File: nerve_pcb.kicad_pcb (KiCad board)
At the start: 6 copper layers, 50 x 50 mm, 81 parts, among them J1 TC2050-IDC, J2 2171750001, J4 472192001, J5 BF030-16A-B1-0360-0277-0600-LB, J6 BF080-20-A-1-L-C, J7 UART, J8 CAN1, J9 CAN2, SW1 SPST, SW2 SPST, U1 ld39150dt33-r, U2 STM32F446RET, U3 TXB0104QPWRQ1, U4 BNO085, U5 BMP390, U6 TJA1051T/3, U7 TJA1051T/3, Y1 8M, Y2 32k768, Y3 32k768

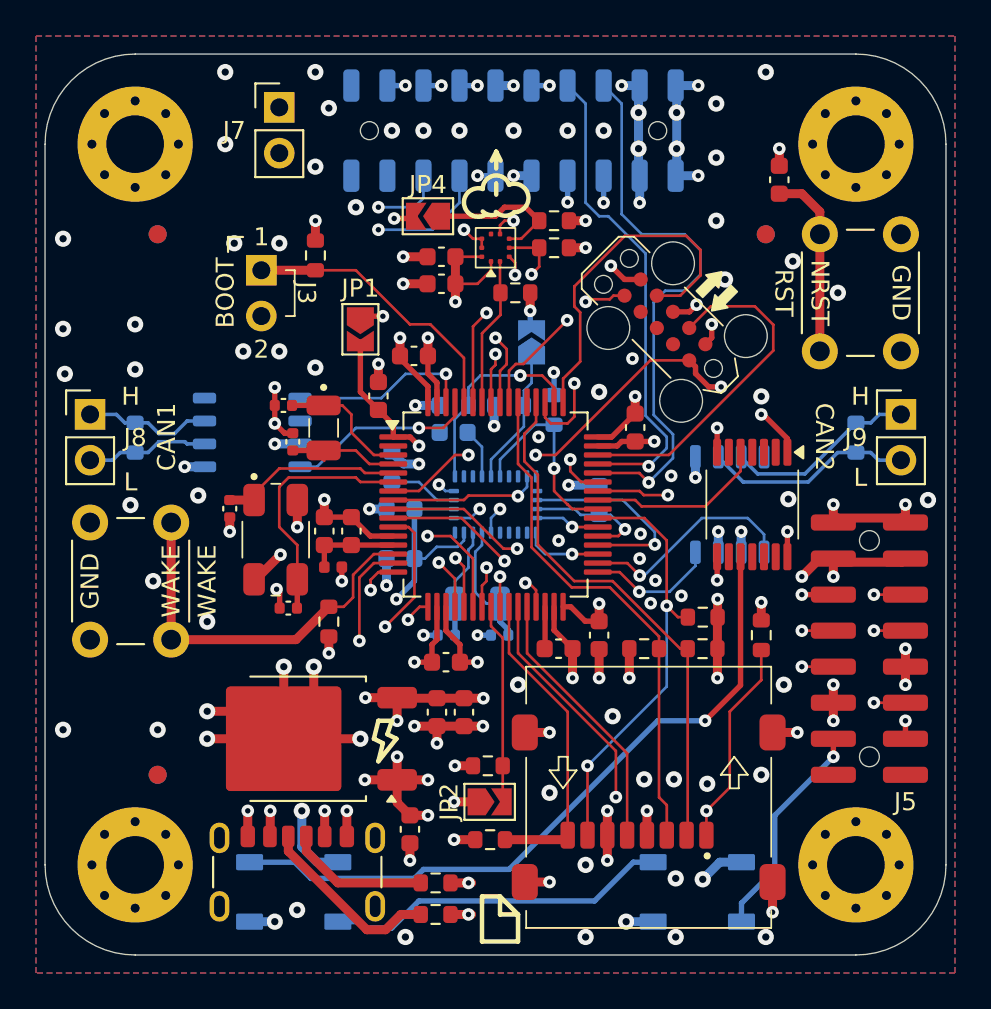
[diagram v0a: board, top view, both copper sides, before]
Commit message: Fix BNO085 circuit and touchups
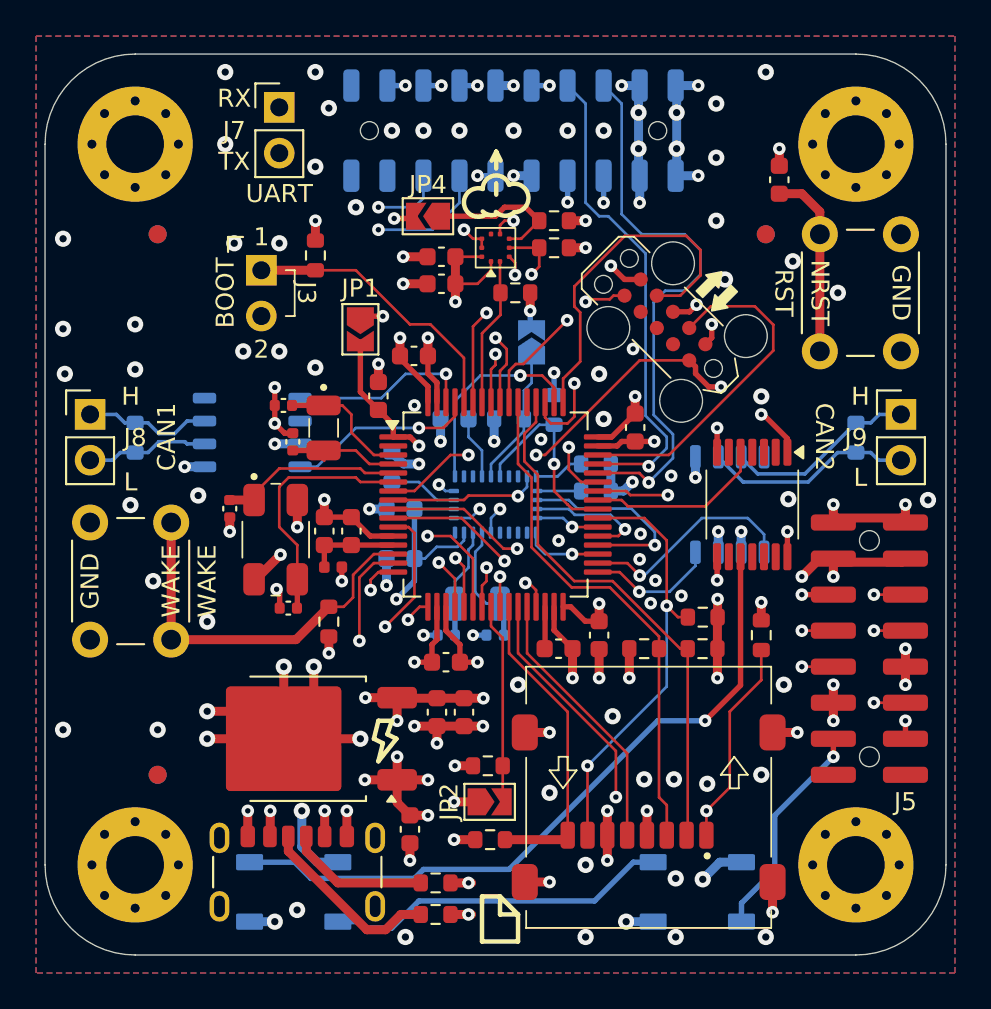
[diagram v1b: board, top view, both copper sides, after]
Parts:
- removed the R11 at (154.2, 104.8)
- added R14: 2k2, Resistor_SMD:R_0603_1608Metric, B.Cu at (154.1, 102.8)
- R15: value 10k -> 2k2
- moved R15 9.22 mm to (154.1, 104.2)
- moved C21 0.75 mm to (146.2, 100.2)
- moved R13 0.75 mm to (149.2, 100.2)
- moved C19 0.25 mm to (148.5, 112.2)
- turned Y3 to 180 degrees
- renumbered C20 to C19, C19 to C20, R13 to R11, R14 to R13
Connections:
- R15 pad 1: /GPIO_IMU_P0 -> +3V3
- R15 pad 2: GND -> Net-(U4-ENV_SDA)
- U4 pad 15: unconnected-(U4-ENV_SCL-Pad15) -> Net-(U4-ENV_SCL)
- U4 pad 16: unconnected-(U4-ENV_SDA-Pad16) -> Net-(U4-ENV_SDA)
- Y3 pad 1: Net-(U4-XIN32) -> Net-(U4-XOUT32/CLKSEL1)
- Y3 pad 2: Net-(U4-XOUT32/CLKSEL1) -> Net-(U4-XIN32)
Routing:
- net Net-(U4-ENV_SCL): track 0.00 -> 2.78 mm
- net Net-(U4-ENV_SDA): track 0.00 -> 2.44 mm
- net +3V3: track 88.7 -> 89.9 mm
- net Net-(U4-CAP): track 2.77 -> 3.50 mm
- net GND: track 102.8 -> 102.9 mm, vias 123 -> 125
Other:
- board text added: "RX"
- board text added: "TX"
- board text added: "UART"

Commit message: Major cleanup and add missing transfer vias
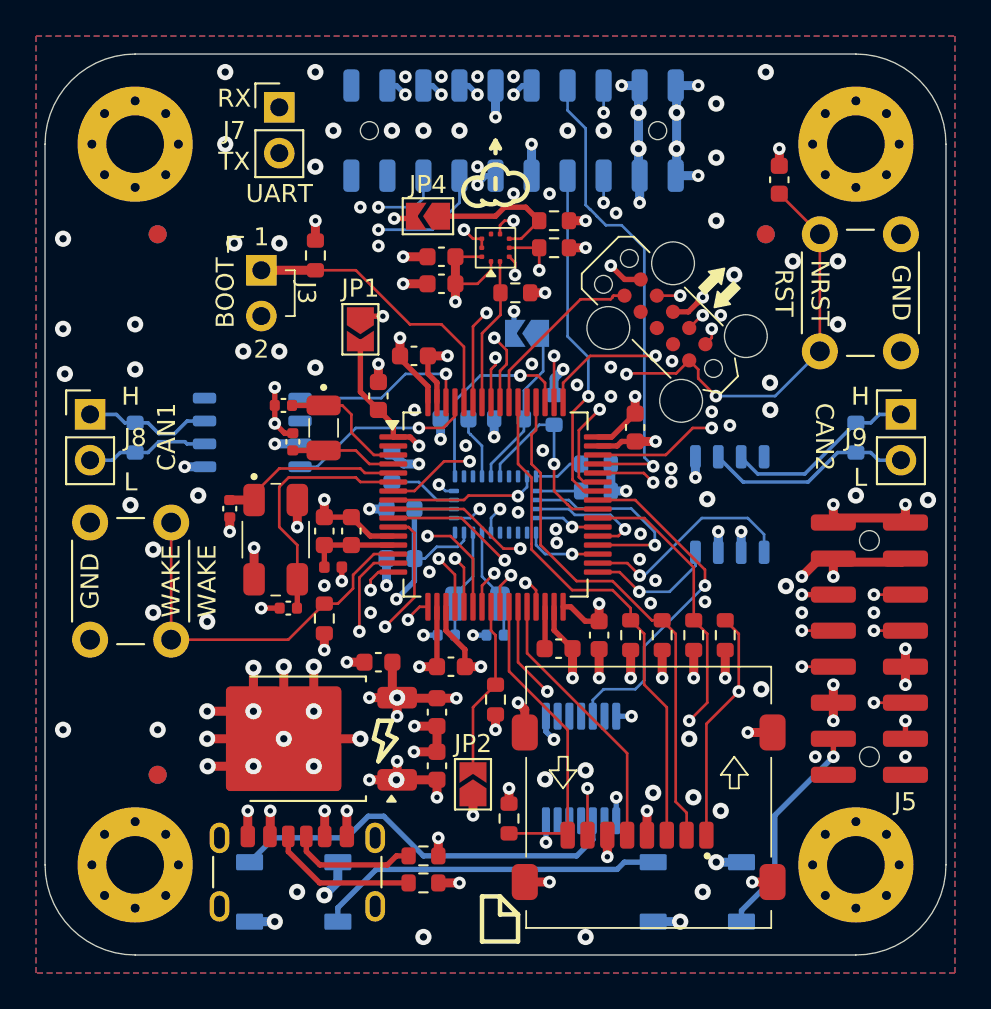
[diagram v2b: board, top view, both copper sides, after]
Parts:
- U3: moved to B.Cu
- moved U3 17.5 mm to (153.2, 119.7)
- moved C9 5.50 mm to (142.0, 113.8), turned to 180 degrees
- moved C3 3.83 mm to (145.2, 119.5), turned to 90 degrees
- moved R10 3.70 mm to (148.5, 115.8), turned to -90 degrees
- moved R7 2.36 mm to (157.8, 112.2), turned to 90 degrees
- moved R8 2.00 mm to (161.2, 112.2), turned to 90 degrees
- moved R2 1.88 mm to (144.5, 126.0)
- moved R1 1.64 mm to (144.5, 124.5)
- moved R4 1.58 mm to (149.2, 122.4), turned to -90 degrees
- moved JP2 1.34 mm to (147.2, 120.5), turned to 90 degrees
- moved R5 1.12 mm to (159.5, 112.2), turned to 90 degrees
- moved R6 1.06 mm to (156.0, 112.2), turned to 90 degrees
- moved JP3 0.56 mm to (150.2, 95.5), turned to 180 degrees
- moved C5 0.37 mm to (146.0, 114.0)
- moved R3 0.31 mm to (139.0, 111.3)
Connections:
- J6 pad 6: /USART1_TX -> /USART1_RX
- J6 pad 8: /USART1_RX -> /USART1_TX
- U2 pad 50: /GPIO_IMU_P0 -> /GPIO_RADIO_RST
- U2 pad 51: /GPIO_RADIO_RST -> /GPIO_IMU_P0
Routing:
- net /TIM1_CH1_PWM_{5V}: track 39.2 -> 22.4 mm, vias 1 -> 0
- net /TIM1_CH1_PWM: track 9.93 -> 19.3 mm, vias 0 -> 1
- net /SWCLK: track 19.7 -> 12.0 mm, vias 0 -> 2
- net +5V: track 35.4 -> 29.6 mm
- net /USART1_CTS: track 31.4 -> 26.7 mm, vias 1 -> 2
- net /USART1_TX: track 24.0 -> 19.4 mm, vias 2 -> 1
- net /SWDIO: track 19.2 -> 15.3 mm, vias 0 -> 2
- net /GPIO_RADIO_RST: track 22.7 -> 19.2 mm
- net GND: track 102.9 -> 106.2 mm, vias 125 -> 155
- net +3V3: track 89.9 -> 87.1 mm, vias 38 -> 40
- net Net-(J2-CC1): track 10.3 -> 8.24 mm
- net /USART2_TX: track 36.1 -> 34.2 mm
- net Net-(JP3-A): track 7.64 -> 9.31 mm
- net /SDIO_D0: track 24.0 -> 25.5 mm
- net /SDIO_DET: track 11.1 -> 9.75 mm
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
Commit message: Cleanup silkscreen
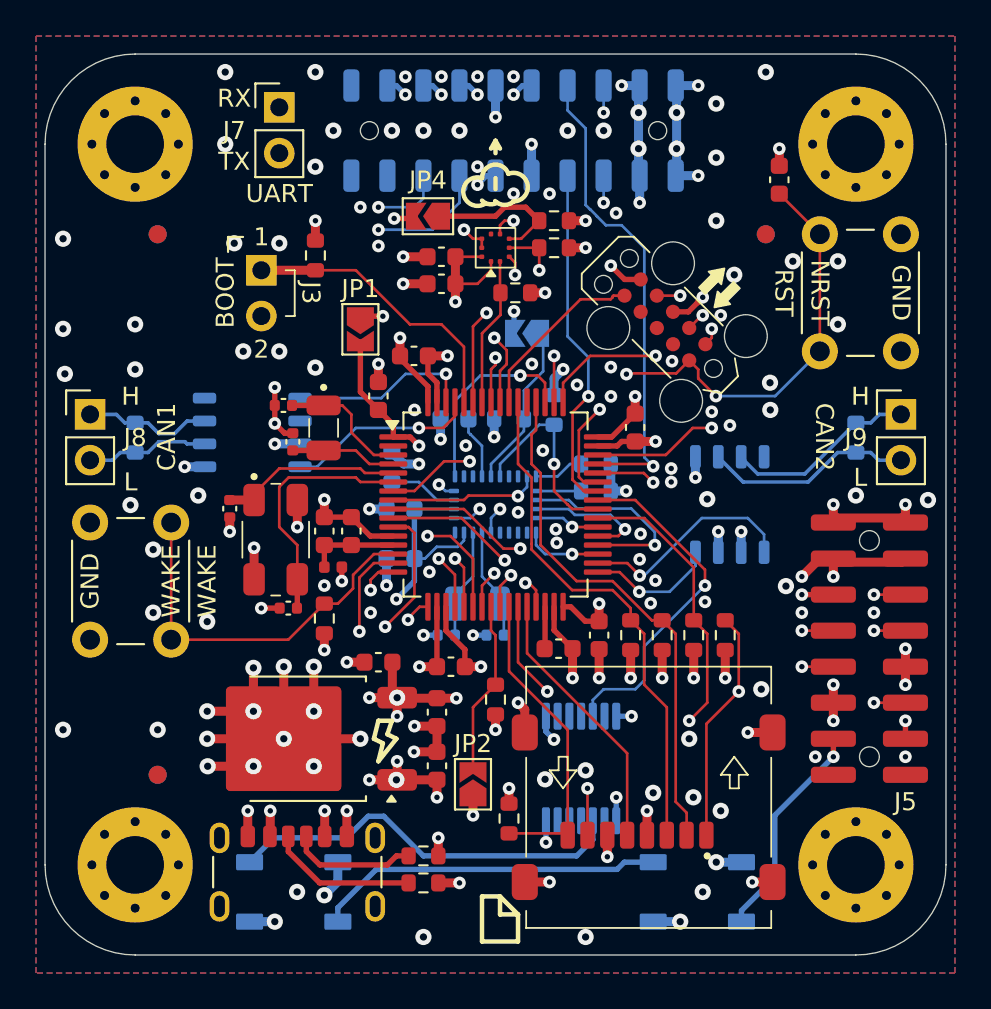
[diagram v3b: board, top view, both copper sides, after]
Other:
- board text added: "Daniel Jeon nerve_pcb v0.1.0-beta"
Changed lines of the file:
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@@
 		(tags "solder jumper open")
 		(property "Reference" "JP1"
-			(at -2.275 0 0)
+			(at -2.25 0 0)
 			(layer "F.SilkS")
 			(effects
@@
 		(tags "solder jumper open")
 		(property "Reference" "JP4"
-			(at 0 1.75 180)
+			(at 0 2 180)
 			(layer "F.SilkS")
 			(effects
@@
 		(tags "resistor")
 		(property "Reference" "R1"
-			(at 2.5 0 360)
+			(at 2.5 0 0)
 			(layer "F.SilkS")
 			(hide yes)
@@
 		)
 		(property "Value" "5k1"
-			(at 2.575 0 360)
+			(at 2.575 0 0)
 			(layer "F.Fab")
 			(effects
@@
 		)
 		(fp_text user "${REFERENCE}"
-			(at 0 0 360)
+			(at 0 0 0)
 			(layer "F.Fab")
 			(effects
@@
 				(font
 					(size 1 1)
-					(thickness 0.1)
+					(thickness 0.15)
 				)
 			)
@@
 		(tags "capacitor")
 		(property "Reference" "C9"
-			(at 2.5 0 360)
+			(at 2.5 0 0)
 			(layer "F.SilkS")
 			(hide yes)
@@
 		)
 		(property "Value" "4u7"
-			(at 2.5 0 360)
+			(at 2.5 0 0)
 			(layer "F.Fab")
 			(effects
@@
 		)
 		(fp_text user "${REFERENCE}"
-			(at 0 0 360)
+			(at 0 0 0)
 			(layer "F.Fab")
 			(effects
@@
 		(at 135.505 93.27 -90)
 		(property "Reference" "J3"
-			(at -0.02 -2.5 -90)
+			(at -0.02 -2.745 -90)
 			(unlocked yes)
 			(layer "F.SilkS")
@@
 				(font
 					(size 1 1)
-					(thickness 0.1)
+					(thickness 0.15)
 				)
 			)
@@
 		(tags "solder jumper open")
 		(property "Reference" "JP3"
-			(at 2.25 0 90)
+			(at 0.25 2 180)
 			(layer "B.SilkS")
 			(effects
@@
 		)
 		(property "Value" "Open"
-			(at 0 0 360)
+			(at 0 0 0)
 			(layer "B.Fab")
 			(effects
@@
 				(font
 					(size 1 1)
-					(thickness 0.1)
+					(thickness 0.15)
 				)
 				(justify mirror)
@@
 	)
 	(gr_text "GND"
-		(at 126 109.25 -90)
+		(at 126 109.25 90)
 		(layer "B.SilkS")
 		(effects
@@
 	)
 	(gr_text "WAKE"
-		(at 130.5 109.25 -90)
+		(at 130.5 109.25 90)
 		(layer "B.SilkS")
 		(effects
@@
 		)
 	)
+	(gr_text "Daniel Jeon\nnerve_pcb\nv0.1.0-beta"
+		(at 148.5 128.75 0)
+		(layer "B.SilkS")
+		(effects
+			(font
+				(size 1 1)
+				(thickness 0.2)
+				(bold yes)
+			)
+			(justify bottom mirror)
+		)
+	)

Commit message: Switch to split CAN termination
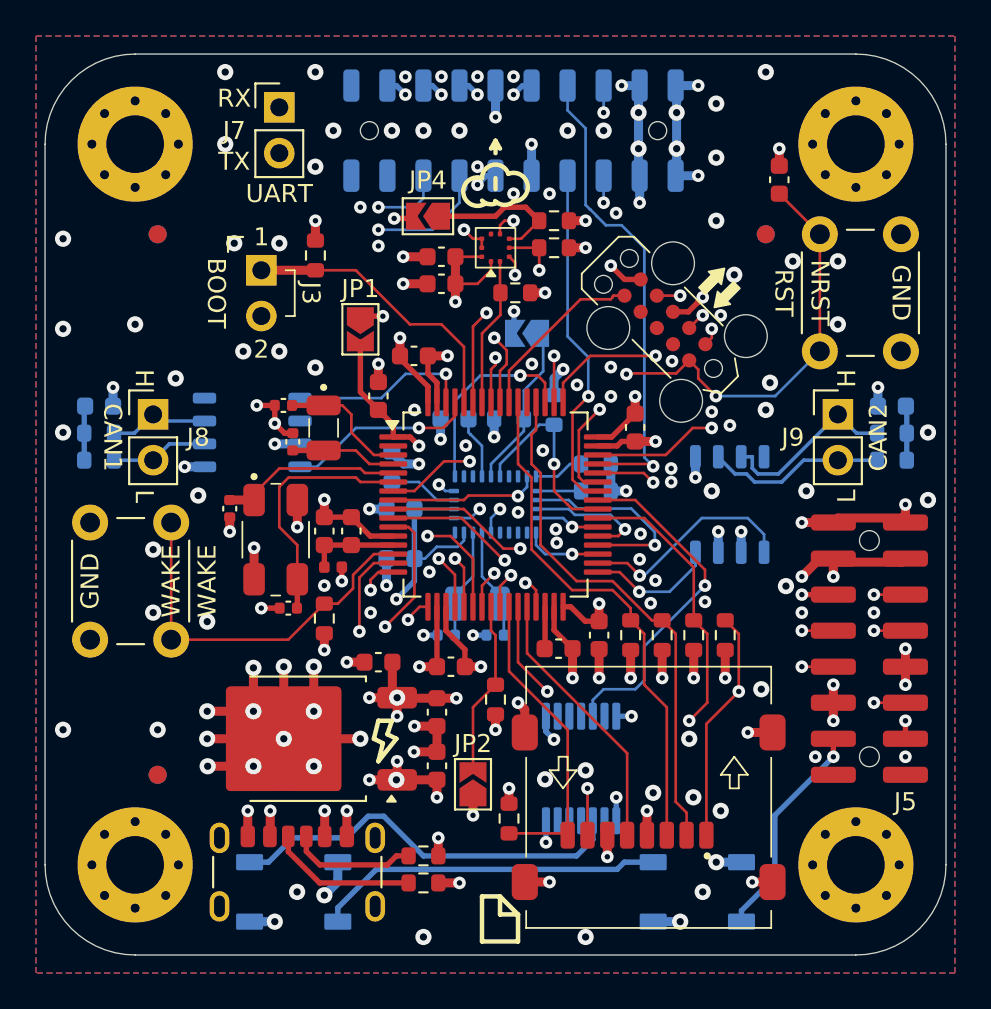
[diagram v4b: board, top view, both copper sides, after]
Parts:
- added C24: 4n7, Capacitor_SMD:C_0603_1608Metric, B.Cu at (126.5, 99.5)
- added C25: 4n7, Capacitor_SMD:C_0603_1608Metric, B.Cu at (170.5, 99.5)
- added R21: 60R, Resistor_SMD:R_0603_1608Metric, B.Cu at (170.5, 102.5)
- added R22: 60R, Resistor_SMD:R_0603_1608Metric, B.Cu at (170.5, 101.0)
- R19, R20: value 120R -> 60R
- moved R20 42.0 mm to (126.5, 101.0), turned to 180 degrees
- moved J8 3.50 mm to (129.5, 100.0)
- moved J9 3.50 mm to (167.5, 100.0)
- moved R19 2.36 mm to (126.5, 102.5), turned to 180 degrees
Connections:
- R19 pad 1: /nerve_pcb_can/CAN1+ -> /nerve_pcb_can/CAN1-
- R19 pad 2: /nerve_pcb_can/CAN1- -> Net-(C24-Pad1)
- R20 pad 1: /nerve_pcb_can/CAN2+ -> /nerve_pcb_can/CAN1+
- R20 pad 2: /nerve_pcb_can/CAN2- -> Net-(C24-Pad1)
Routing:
- net Net-(C24-Pad1): track 0.00 -> 3.02 mm
- net Net-(C25-Pad1): track 0.00 -> 3.02 mm
- net GND: track 106.2 -> 108.3 mm, vias 155 -> 157
- net /nerve_pcb_can/CAN2-: track 11.6 -> 9.90 mm
- net /nerve_pcb_can/CAN1+: track 7.08 -> 5.61 mm
- net /nerve_pcb_can/CAN1-: track 6.82 -> 5.40 mm
- net +5V: track 29.6 -> 30.3 mm
- net /nerve_pcb_can/CAN2+: track 10.6 -> 10.1 mm
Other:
- board text added: "Daniel Jeon nerve_pcb v0.1.0"
- board text removed: "Daniel Jeon nerve_pcb v0.1.0-beta"

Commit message: Update IMU silkscreen graphic
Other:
- board text added: "X"
- board text added: "Y"
- board text added: "Z"
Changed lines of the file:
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@@
 	)
 	(gr_line
-		(start 151.666514 110.172935)
-		(end 151.111162 110.109021)
-		(stroke
-			(width 0.25)
-			(type default)
-		)
-		(layer "B.SilkS")
-	)
-	(gr_line
-		(start 151.625548 108.541504)
-		(end 151.317537 108.074998)
-		(stroke
-			(width 0.25)
-			(type default)
-		)
-		(layer "B.SilkS")
-	)
-	(gr_line
-		(start 153.388838 110.140978)
-		(end 153.388838 107.039186)
-		(stroke
-			(width 0.25)
-			(type default)
-		)
-		(layer "B.SilkS")
-	)
-	(gr_line
-		(start 154.388838 108.890978)
-		(end 151.111162 110.109021)
-		(stroke
-			(width 0.25)
-			(type default)
-		)
-		(layer "B.SilkS")
-	)
-	(gr_line
-		(start 153.138838 107.539186)
-		(end 153.388838 107.039186)
-		(stroke
-			(width 0.25)
-			(type default)
-		)
-		(layer "B.SilkS")
-	)
-	(gr_line
-		(start 154.198142 109.8)
-		(end 151.317537 108.074998)
-		(stroke
-			(width 0.25)
-			(type default)
-		)
-		(layer "B.SilkS")
-	)
-	(gr_line
-		(start 153.638838 107.539186)
-		(end 153.388838 107.039186)
-		(stroke
-			(width 0.25)
-			(type default)
-		)
-		(layer "B.SilkS")
-	)
-	(gr_line
-		(start 151.87555 108.108493)
-		(end 151.317537 108.074998)
-		(stroke
-			(width 0.25)
-			(type default)
-		)
-		(layer "B.SilkS")
-	)
-	(gr_line
-		(start 151.495504 109.703088)
-		(end 151.111162 110.109021)
+		(start 151 110)
+		(end 151.5 110.5)
+		(stroke
+			(width 0.25)
+			(type default)
+		)
+		(layer "B.SilkS")
+	)
+	(gr_line
+		(start 153.5 108.5)
+		(end 153 109)
+		(stroke
+			(width 0.25)
+			(type default)
+		)
+		(layer "B.SilkS")
+	)
+	(gr_line
+		(start 153.5 108.5)
+		(end 152.5 108.5)
+		(stroke
+			(width 0.25)
+			(type default)
+		)
+		(layer "B.SilkS")
+	)
+	(gr_circle
+		(center 151.5 108.5)
+		(end 152.5 108.5)
+		(stroke
+			(width 0.25)
+			(type default)
+		)
+		(fill none)
+		(layer "B.SilkS")
+	)
+	(gr_line
+		(start 152 110)
+		(end 151.5 110.5)
+		(stroke
+			(width 0.25)
+			(type default)
+		)
+		(layer "B.SilkS")
+	)
+	(gr_line
+		(start 151.5 109.5)
+		(end 151.5 110.5)
+		(stroke
+			(width 0.25)
+			(type default)
+		)
+		(layer "B.SilkS")
+	)
+	(gr_line
+		(start 153 108)
+		(end 153.5 108.5)
 		(stroke
 			(width 0.25)
@@
 		)
 	)
+	(gr_text "Z"
+		(at 151.5 108.5 0)
+		(layer "B.SilkS")
+		(effects
+			(font
+				(size 1 1)
+				(thickness 0.25)
+				(bold yes)
+			)
+			(justify mirror)
+		)
+	)
 	(gr_text "L"
 		(at 168.04 104.54 90)
@@
 		)
 	)
+	(gr_text "X"
+		(at 154.25 108.5 0)
+		(layer "B.SilkS")
+		(effects
+			(font
+				(size 1 1)
+				(thickness 0.25)
+				(bold yes)
+			)
+			(justify mirror)
+		)
+	)
 	(gr_text "WAKE"
 		(at 130.5 109.25 90)
@@
 			)
 			(justify mirror)
+		)
+	)
+	(gr_text "Y"
+		(at 151.5 111.5 0)
+		(layer "B.SilkS")
+		(effects
+			(font
+				(size 1 1)
+				(thickness 0.25)
+				(bold yes)
+			)
+			(justify mirror)
